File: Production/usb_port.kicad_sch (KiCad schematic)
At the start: 83 parts, among them J401 TYPE-C 16PCB0.8 IP68, Q401 SiZ240DT, Q402 SiZ240DT, U401 TPS25751DREFR, U402 M24512-DFMC6TG, U403 BQ25756RRVR, U404 TPS62933DRLR, U405 TPD4S201TRGRRQ1

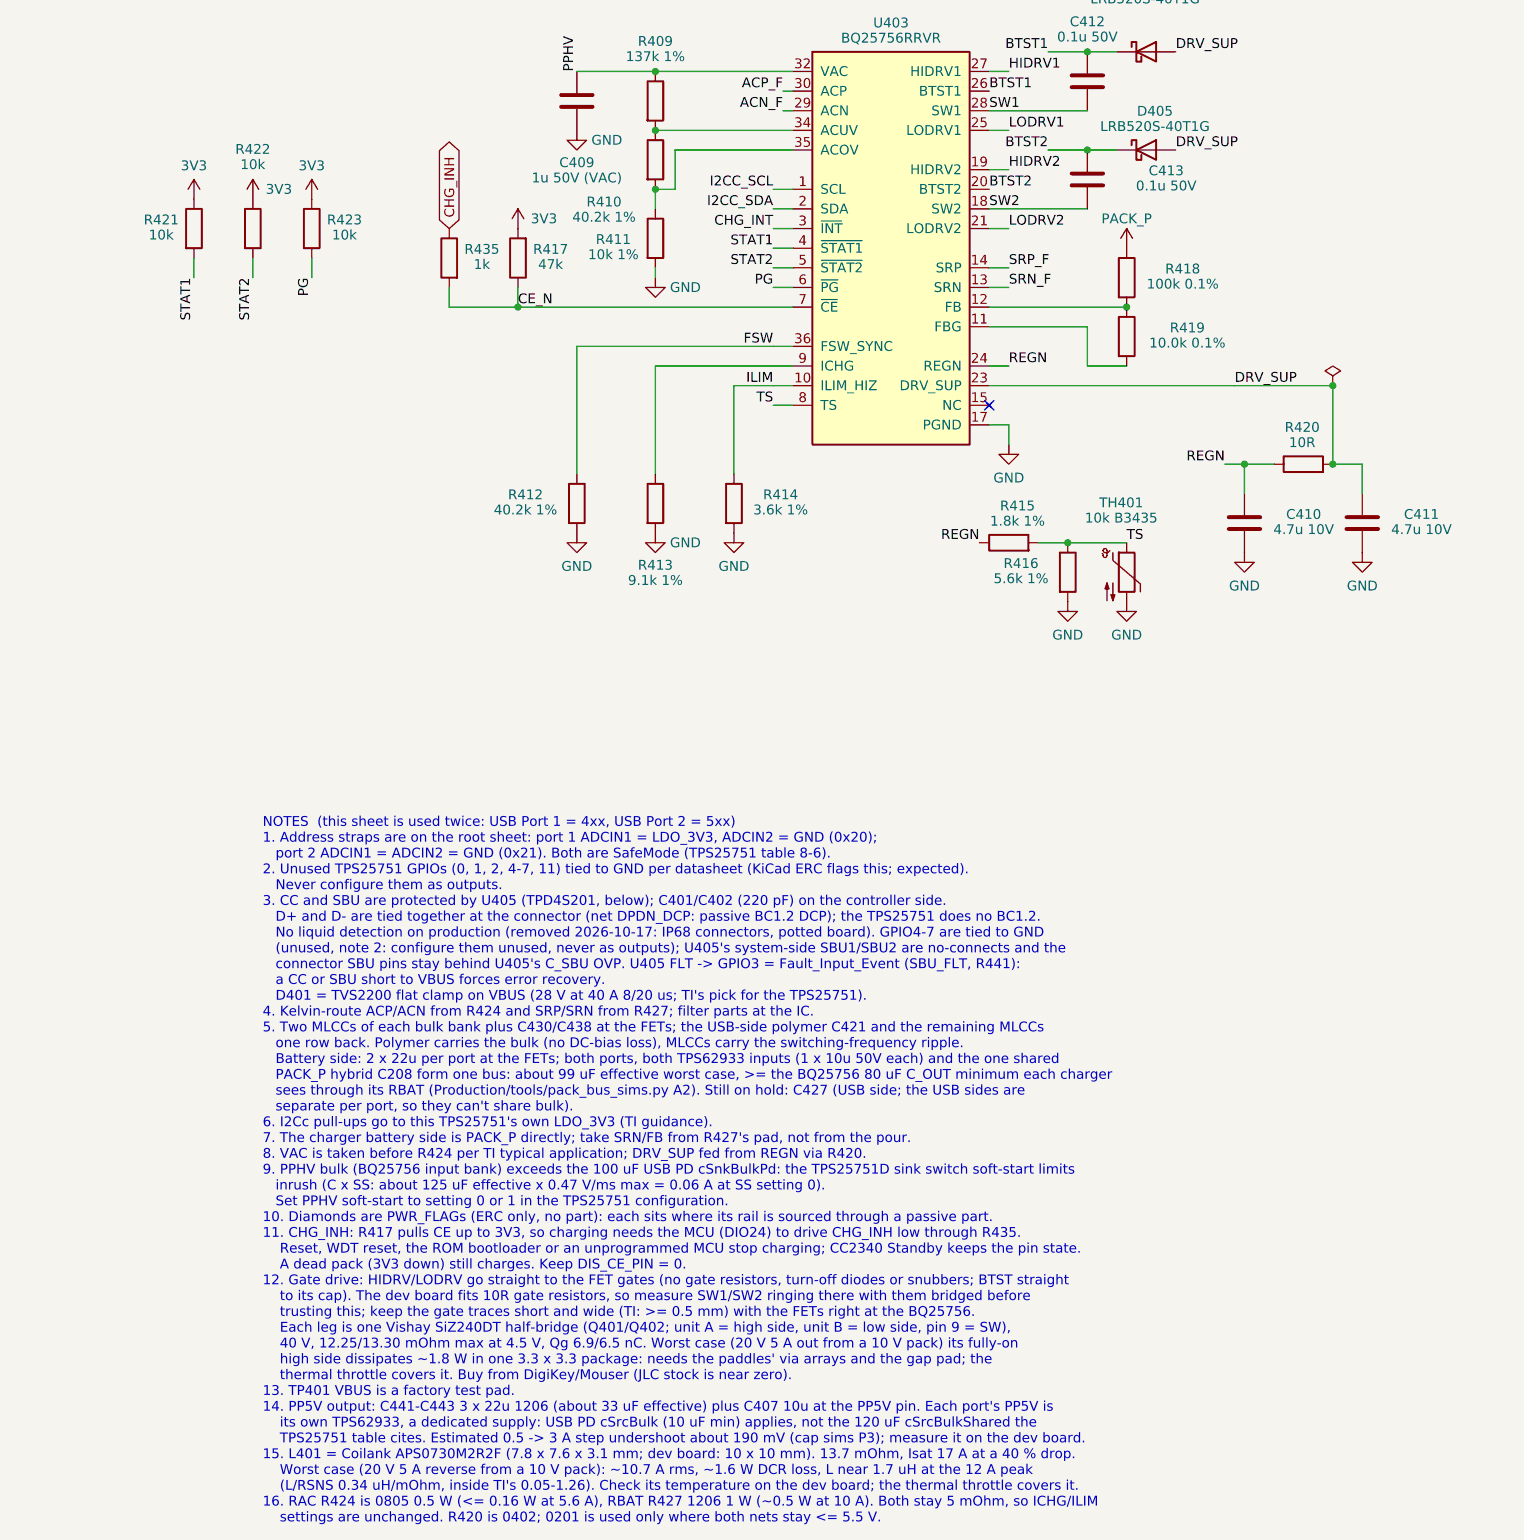
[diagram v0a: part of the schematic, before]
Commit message: Production schematic P0: remove BQ25756 STAT1/STAT2/PG pull-ups
R421-R423 and R521-R523 removed; U403/U503 pins 4-6 no-connect (open-drain,
unused: status over I2C). Set DIS_STAT_PINS = 1. Netlist check passes.

Co-Authored-By: Claude Opus 5.5 <noreply@anthropic.com>
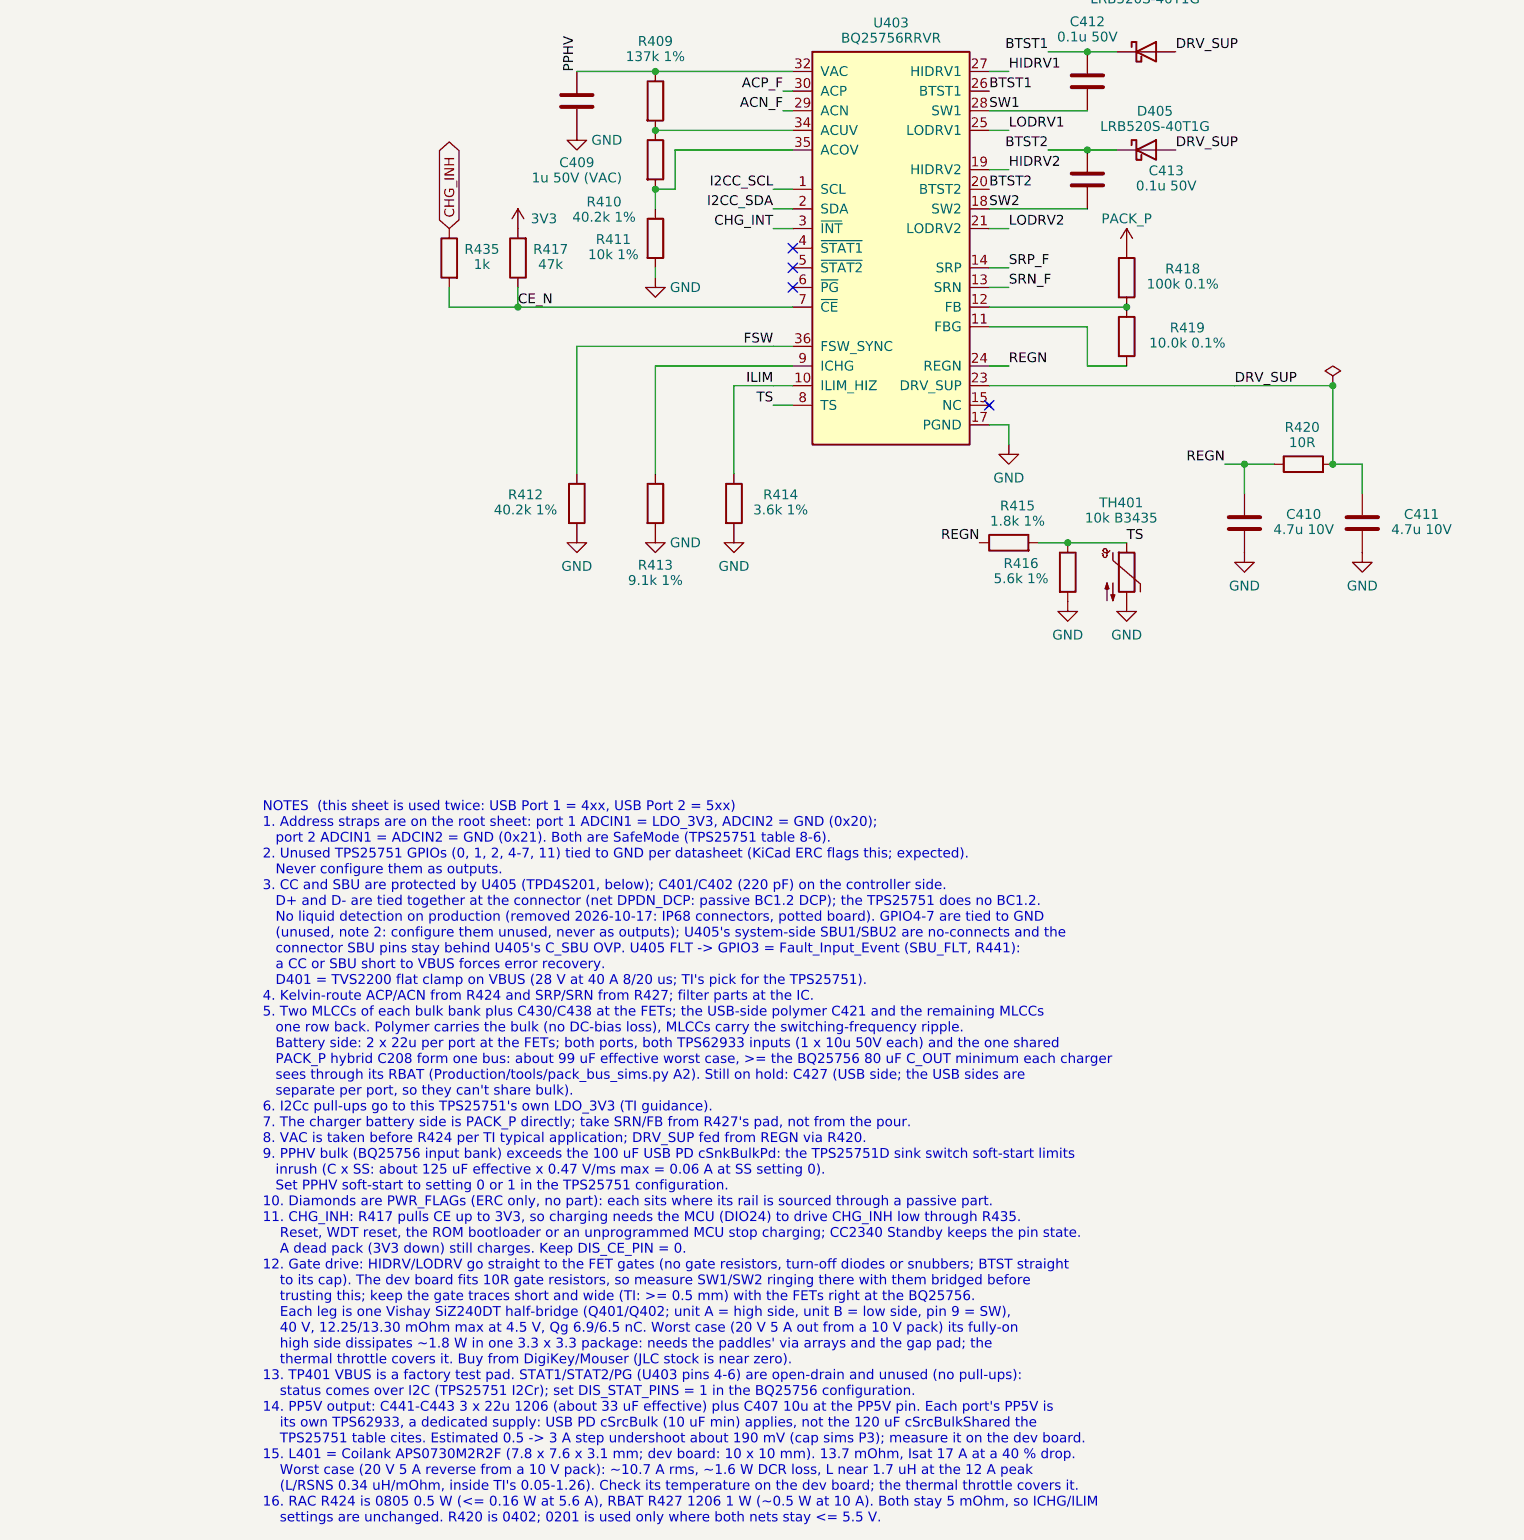
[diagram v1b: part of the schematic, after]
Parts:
- removed R421, R422, R423: 10k, Resistor_SMD:R_0201_0603Metric, symbol Device:R
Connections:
- net PG: no longer names the net of U403.6 (~{PG})
- net STAT1: no longer names the net of U403.4 (~{STAT1})
- net STAT2: no longer names the net of U403.5 (~{STAT2})
- no-connect marks 3 -> 6

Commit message: Production schematic P0: U405/U505 TPD4S201 -> TPD2S300 (CC only)
CC keeps short-to-VBUS OVP and IEC ESD (TPS25751 CC pins are only +-1 kV
HBM); SBU half dropped with liquid detection, connector SBU pins no-connect.
VPWR/VM on LDO_3V3, VBIAS C451, FLT -> GPIO3. tools/tpd2s300.py. Netlist check
passes; ERC unchanged. Courtyard 1923 -> 1884 mm2.

Co-Authored-By: Claude Opus 5.5 <noreply@anthropic.com>
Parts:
- removed U405: TPD4S201TRGRRQ1, MonolithDev:TI_RGR0020C_VQFN-20-1EP_3.5x3.5mm_P0.5mm_EP2.05mm, symbol MonolithDev:TPD4S201
- added U405: TPD2S300YFFR, MonolithDev:TI_YFF0009_DSBGA-9_P0.4mm, symbol MonolithDev:TPD2S300
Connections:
- net CC1: now also U405.B1 (CC1)
- net CC2: now also U405.B3 (CC2)
- net C_CC1: now also U405.A1 (C_CC1)
- net C_CC2: now also U405.A3 (C_CC2)
- net GND: now also U405.B2 (GND)
- net LDO_3V3: now also U405.C2 (VPWR), U405.C3 (VM)
- net SBU_FLT: now also U405.C1 (~{FLT})
- net VBIAS: now reaches C451.1
- net VBIAS: now also U405.A2 (VBIAS)
- net SBU1: no longer names the net of J401.A8 (SBU1)
- net SBU2: no longer names the net of J401.B8 (SBU2)
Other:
- note added: "CC PROTECTION (TPD2S300)"
- note added: "NOTES (this sheet is used twice: USB Port 1 = 4xx, USB Port 2 = 5xx) 1. Address straps are on the root sheet: port 1 ADCIN1 = LDO_3V3, ADCIN2 = GND (0x20); port 2 ADCIN1 = ADCIN2 = GND (0x21). Both are SafeMode (TPS25751 table 8-6). 2. Unused TPS25751 GPIOs (0, 1, 2, 4-7, 11) tied to GND per datasheet (KiCad ERC flags this; expected). Never configure them as outputs. 3. CC is protected by U405 (T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"
- note removed: "CC/SBU PROTECTION (TPD4S201)"
- note removed: "NOTES (this sheet is used twice: USB Port 1 = 4xx, USB Port 2 = 5xx) 1. Address straps are on the root sheet: port 1 ADCIN1 = LDO_3V3, ADCIN2 = GND (0x20); port 2 ADCIN1 = ADCIN2 = GND (0x21). Both are SafeMode (TPS25751 table 8-6). 2. Unused TPS25751 GPIOs (0, 1, 2, 4-7, 11) tied to GND per datasheet (KiCad ERC flags this; expected). Never configure them as outputs. 3. CC and SBU are protected b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"

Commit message: Production P0 is the first build: gauge training access and tuning hedges
Dev board skipped. J302 = second TC2030-NL (GAUGE: SDA, CHG_INH, NRST, GND,
SCL) replacing the SMBus pogo pads; J113/J114 PACK_P/GND load pads for the
learning cycle; R118 4.7k + TP113 WAKE pad. Hedges: R444-R447 back as 0R
0402 gate links, DNP 0402 snubbers. Probe pads (1.0 mm) VBUS/PPHV/PP5V/REGN/
SW1/SW2/GND per port. docs/production/p0-bringup-and-training.md. Netlist
check passes; ERC known warnings only. Board/.kicad_pro (user WIP) not included.

Co-Authored-By: Claude Opus 5.5 <noreply@anthropic.com>
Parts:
- added C454, C455: 33p C0G, Capacitor_SMD:C_0402_1005Metric, symbol Device:C
- added R444, R445, R446, R447: 0R, Resistor_SMD:R_0402_1005Metric, symbol Device:R
- added R450, R451: 3R3, Resistor_SMD:R_0402_1005Metric, symbol Device:R
- added TP402: PPHV, TestPoint:TestPoint_Pad_D1.0mm, symbol Connector:TestPoint
- added TP403: PP5V, TestPoint:TestPoint_Pad_D1.0mm, symbol Connector:TestPoint
- added TP404: REGN, TestPoint:TestPoint_Pad_D1.0mm, symbol Connector:TestPoint
- added TP405: SW1, TestPoint:TestPoint_Pad_D1.0mm, symbol Connector:TestPoint
- added TP406: SW2, TestPoint:TestPoint_Pad_D1.0mm, symbol Connector:TestPoint
- added TP412: GND, TestPoint:TestPoint_Pad_D1.0mm, symbol Connector:TestPoint
- TP401: footprint TestPoint:TestPoint_Pad_D1.5mm -> TestPoint:TestPoint_Pad_D1.0mm
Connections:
- net GND: now also C454.2, C455.2, TP412.1
- net HIDRV1: now also R444.1; no longer Q401.1 (G1)
- net HIDRV2: now also R446.1; no longer Q402.1 (G1)
- net LODRV1: now also R445.1; no longer Q401.8 (G2)
- net LODRV2: now also R447.1; no longer Q402.8 (G2)
- net PP5V: now also TP403.1
- net PPHV: now also TP402.1
- net REGN: now also TP404.1
- net SW1: now also R450.1, TP405.1
- net SW2: now also R451.1, TP406.1
- new net: C454.1, R450.2
- new net: C455.1, R451.2
- new net HG1: Q401.1 (G1), R444.2
- new net HG2: Q402.1 (G1), R446.2
- new net LG1: Q401.8 (G2), R445.2
- new net LG2: Q402.8 (G2), R447.2
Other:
- note added: "GATE LINKS (0R, fitted) + SNUBBERS (DNP): P0 tuning hedge"
- note added: "PROBE PADS (1.0 mm): VBUS PPHV PP5V REGN SW1 SW2 + GND"
- note removed: "FACTORY TEST PAD"

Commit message: Production schematic P0: layout clean-up pass
New tools/layout_production.py (after make and tidy): block moves via
DevBoard/tools/move_region.py, then place_fields.py and check_overlaps.py.
Gauge: pack/NTC pads compacted, current sense and test/training pads moved up;
MCU: blocks regrouped, notes moved, J302 at 5.08 mm pin pitch; 3V3 Rail:
shared bulk and notes beside the rail; stale headings and index text fixed.
0 overlaps on all sheets; netlist check passes; ERC known warnings only.

Co-Authored-By: Claude Opus 5.5 <noreply@anthropic.com>
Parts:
- R424: value 5m 0.5W (RAC) -> 5m 0.5W; Notes (none) -> RAC

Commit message: Production board: side outline and 1.6 mm thickness (for cost)
- Monolith.kicad_pcb: 43.2 x 74.35 mm side-board outline with bottom
  corners notched around the tray's screw pillars; J501/J401 on the top
  edge at x 93.5 / 106.5, 180 deg, locked. Stack-up 6 layers 1.6 mm
  (symmetric approximation; use JLC's stack at order time).
- make_board.py imports the outline from mechanical/monolith_shell.py
  (one source for tray and board). New --keep-copper flag: the four
  hand-drawn VBUS traces near the old J401 position are kept as they
  were and now dangle.
- J401/J501: TYPE-C 16PCB1.6 IP68 (C55629729) in the schematic, board
  and make_production.py; same land pattern as the 0.8 mm part.
- mechanical: SB_PCB_T = 1.6, USB-C centreline derived from it; the
  pack is 0.8 mm wider (55.2 x 49.0 x 83.0 with bumpers, ~338 g). All
  assembly checks pass; STLs and render regenerated.
- Docs: Production README (stack-up, JLC via limits at 1.6 mm, new
  side-outline section, history notes), root README, next-actions log.

DRC: no outline errors; remaining items are the known pending schematic
update, the TPD2S300 via-in-pad and the 3 dangling VBUS traces.

Co-Authored-By: Claude Opus 5.5 <noreply@anthropic.com>
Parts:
- J401: value TYPE-C 16PCB0.8 IP68 -> TYPE-C 16PCB1.6 IP68; footprint MonolithDev:USB_C_Receptacle_ShouHan_TYPE-C_16PCB0.8_IP68 -> MonolithDev:USB_C_Receptacle_ShouHan_TYPE-C_16PCB1.6_IP68; LCSC C55629727 -> C55629729; MPN TYPE-C 16PCB0.8 IP68 (Shou Han) -> TYPE-C 16PCB1.6 IP68 (Shou Han)
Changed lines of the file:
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@@
 			)
 		)
-		(property "Value" "TYPE-C 16PCB0.8 IP68"
+		(property "Value" "TYPE-C 16PCB1.6 IP68"
 			(at 45.72 76.96 0)
 			(show_name no)
@@
 			)
 		)
-		(property "Footprint" "MonolithDev:USB_C_Receptacle_ShouHan_TYPE-C_16PCB0.8_IP68"
+		(property "Footprint" "MonolithDev:USB_C_Receptacle_ShouHan_TYPE-C_16PCB1.6_IP68"
 			(at 49.53 96.52 0)
 			(hide yes)
@@
 			)
 		)
-		(property "LCSC" "C55629727"
+		(property "LCSC" "C55629729"
 			(at 45.72 96.52 0)
 			(hide yes)
@@
 			)
 		)
-		(property "MPN" "TYPE-C 16PCB0.8 IP68 (Shou Han)"
+		(property "MPN" "TYPE-C 16PCB1.6 IP68 (Shou Han)"
 			(at 45.72 96.52 0)
 			(hide yes)

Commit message: Production: U405/U505 TPD2S300 -> TPD6S300 (no via-in-pad)
The TPD2S300's WCSP-9 centre ball needed a 0.15 mm via-in-pad, below
JLC's no-surcharge hole size and the project's 0.3 mm drill rule. The
TPD6S300RUKR (WQFN-20 3x3, LCSC C2649810) does the same CC job
(24 V short-to-VBUS OVP, IEC ESD, FLT) and fans out with standard vias.

- tools/tpd6s300.py: symbol, pin nets, and a footprint from KiCad's
  RUK0020B with four 0.3/0.5 mm vias in the exposed pad
- RPD_G1/G2 -> C_CC1/C_CC2 for dead-battery Rd; SBU and D1/D2 unused
- board: footprints swapped in place, U405 moved 0.65 mm clear of U401
- IVPWR is 90 uA typ per part (TPD2S300: 3.2 uA), noted in the README

Co-Authored-By: Claude Opus 5.5 <noreply@anthropic.com>
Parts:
- removed U405: TPD2S300YFFR, MonolithDev:TI_YFF0009_DSBGA-9_P0.4mm, symbol MonolithDev:TPD2S300
- added U405: TPD6S300RUKR, MonolithDev:TI_RUK0020B_WQFN-20-1EP_3x3mm_P0.4mm_EP1.7x1.7mm_Via0.3, symbol MonolithDev:TPD6S300
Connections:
- net CC1: now also U405.12 (CC1)
- net CC2: now also U405.11 (CC2)
- net C_CC1: now also U405.4 (C_CC1), U405.8 (RPD_G1)
- net C_CC2: now also U405.5 (C_CC2), U405.6 (RPD_G2)
- net GND: now also U405.13 (GND), U405.16 (N.C.), U405.17 (N.C.), U405.18 (GND), U405.21 (GND), U405.7 (GND)
- net LDO_3V3: now also U405.10 (VPWR)
- net SBU_FLT: now also U405.9 (~{FLT})
- net VBIAS: now also U405.3 (VBIAS)
- no-connect marks 6 -> 12
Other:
- note added: "CC PROTECTION (TPD6S300)"
- note removed: "CC PROTECTION (TPD2S300)"

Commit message: Production: low-profile bulk, nothing taller than the 3.1 mm inductors
USB side per port: C421 100u can -> KEMET T521D 33u 35V polymer tantalum,
plus C457 (second T521D) and C456 (fifth 22u 35V 1210): 83 uF worst at 20 V.
PACK_P: C208 hybrid -> C208-C213, six GMK325 22u 35V 1210; C431/C434/C444 ->
the same part: 86 uF worst at 16.8 V, all MLCC (polymer chips' leakage
rating is too high for the always-live bus). C427 leaves the cut list.
Checked with tools/low_profile_sims.py (options L2 / N1).

Co-Authored-By: Claude Opus 5.5 <noreply@anthropic.com>
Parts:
- added C456: 22u 35V, Capacitor_SMD:C_1210_3225Metric, symbol Device:C
- added C457: 33u 35V, Capacitor_Tantalum_SMD:CP_EIA-7343-31_Kemet-D, symbol Device:C_Polarized
- C421: value 100u 35V -> 33u 35V; footprint Capacitor_SMD:CP_Elec_6.3x7.7 -> Capacitor_Tantalum_SMD:CP_EIA-7343-31_Kemet-D; LCSC C5246554 -> C696815; MPN Honor Elec HV1V107M0607PZ (polymer) -> KEMET T521D336M035ATE065 (polymer tantalum); Notes USB-side bulk, polymer (no DC-bias loss). 100 uF (was 68 uF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 -> USB-side bulk with C457 (two 33 uF polymer tantalum, 65 mOh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
- C431, C434: value 22u 25V -> 22u 35V; footprint Capacitor_SMD:C_1206_3216Metric -> Capacitor_SMD:C_1210_3225Metric; LCSC C12891 -> C778721; MPN CL31A226KAHNNNE -> GMK325BJ226MM-P; Notes Battery-side ripple MLCC (C431/C434/C435 and C531/C534/C535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 -> Battery-side MLCC at the charger FETs, 22u 35V 1210 (about 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
- C444: value 10u 50V -> 22u 35V; footprint Capacitor_SMD:C_1206_3216Metric -> Capacitor_SMD:C_1210_3225Metric; LCSC C13585 -> C778721; MPN CL31A106KBHNNNE -> GMK325BJ226MM-P
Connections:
- net AC_SNS_N: now also C456.1, C457.1
- net GND: now also C456.2, C457.2
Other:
- note added: "BATTERY-SIDE LOCAL: 2 x 22u 35V 1210; shared PACK_P bulk C208-C213 (3V3 Rail sheet)"
- note removed: "BATTERY-SIDE LOCAL: 2 x 22u MLCC; bulk is the shared PACK_P hybrid C208 (3V3 Rail sheet)"
